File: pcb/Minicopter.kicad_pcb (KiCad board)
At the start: 2 copper layers, 57 parts, among them J1 USB_C_Receptacle_USB2.0_16P, J2 Conn_01x02, J3 Conn_01x02_Socket, J4 Conn_01x02_Socket, J5 Conn_01x02_Socket, J6 Conn_01x02_Socket, Q1 AO3401A, SW1 SS-12D00, T1 IRLML6344TRPBF, T2 IRLML6344TRPBF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

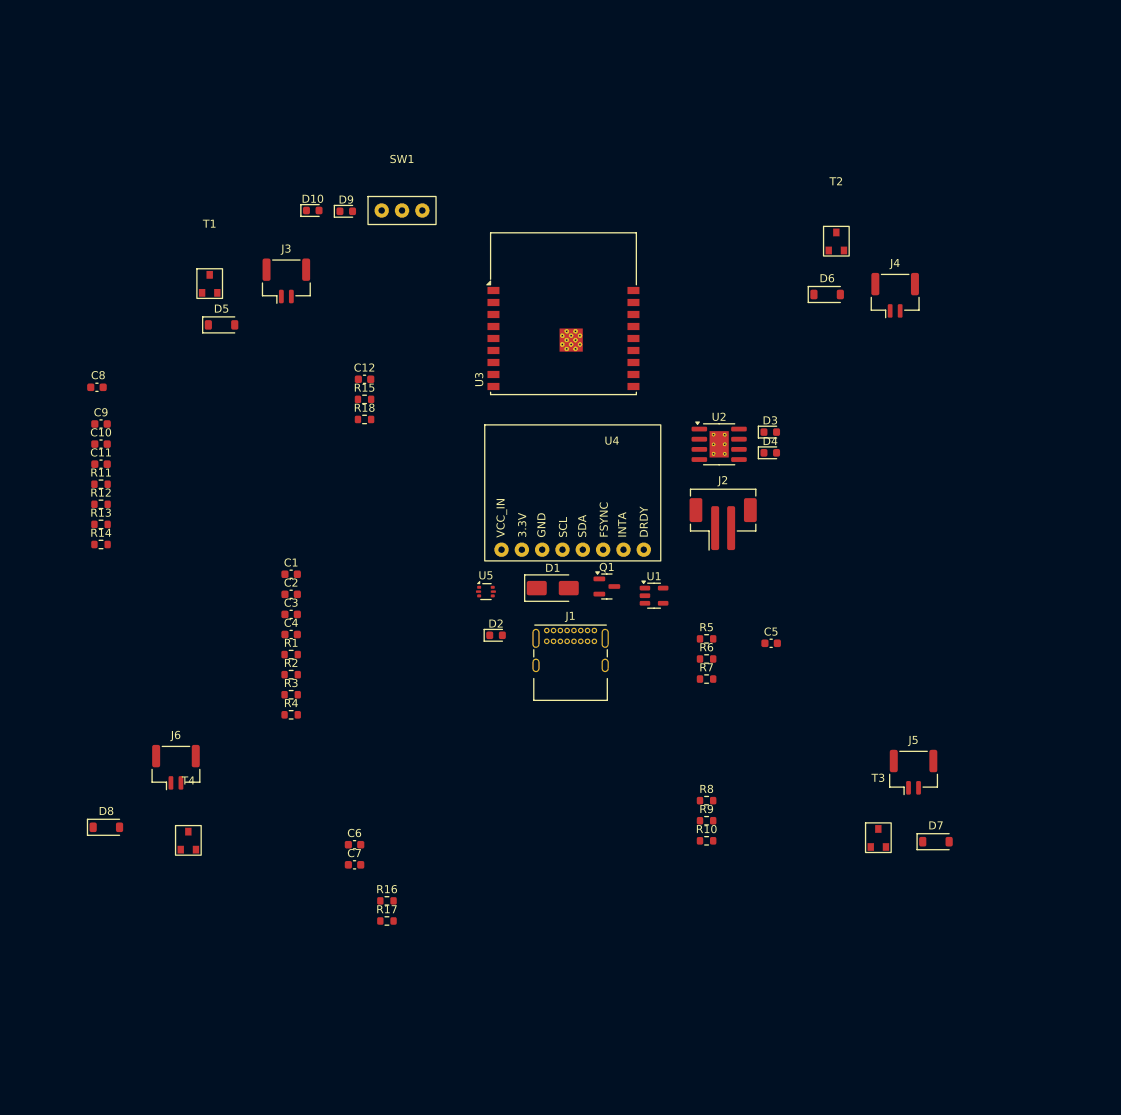
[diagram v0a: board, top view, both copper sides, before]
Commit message: without gnd
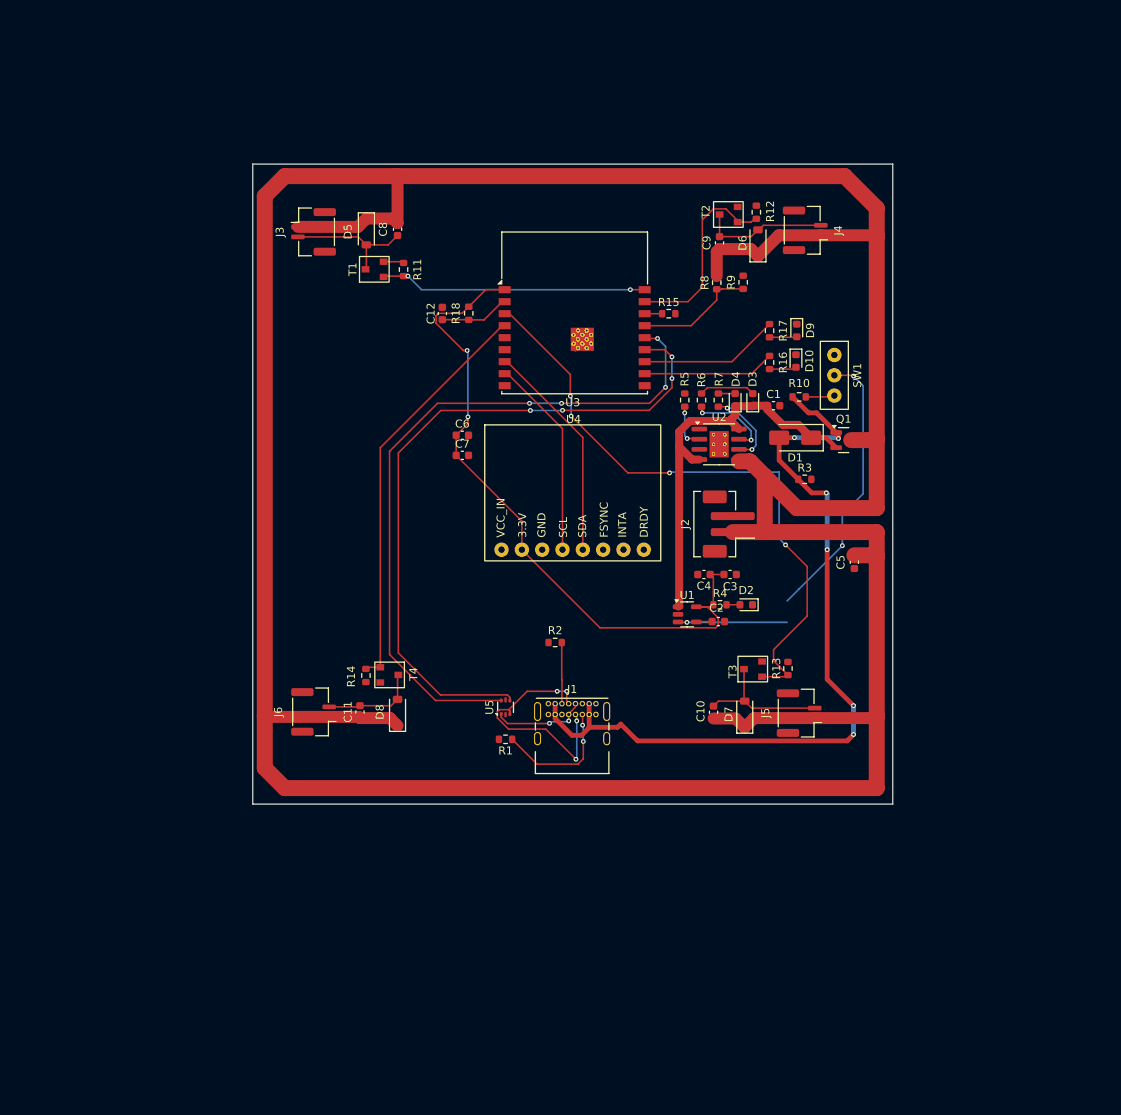
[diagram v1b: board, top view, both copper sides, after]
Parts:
- moved R12 89.7 mm to (173.9, 52.0), turned to 90 degrees
- moved R17 87.9 mm to (175.6, 66.8), turned to -90 degrees
- moved R13 87.7 mm to (177.9, 109.0), turned to 90 degrees
- moved C10 83.6 mm to (168.6, 114.5), turned to 90 degrees
- moved R16 82.6 mm to (175.6, 70.8), turned to -90 degrees
- moved C9 80.6 mm to (169.3, 55.8), turned to 90 degrees
- moved R3 69.6 mm to (180.0, 85.4)
- moved R9 67.5 mm to (172.3, 60.8), turned to -90 degrees
- moved R8 64.8 mm to (169.0, 60.8), turned to -90 degrees
- moved C1 63.9 mm to (176.1, 76.2)
- moved D10 63.3 mm to (178.9, 70.6), turned to -90 degrees
- moved D9 58.2 mm to (179.0, 66.8), turned to -90 degrees
- moved SW1 57.8 mm to (183.7, 72.4), turned to -90 degrees
- moved R10 56.7 mm to (179.3, 75.1)
- moved R4 55.3 mm to (169.4, 101.1)
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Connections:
- C1 pad 1: VBUS -> +5V
- D1 pad 1: VBUS -> +5V
- D1 pad 2: +5V -> VBUS
- J1 pad A4: +5V -> VBUS
- J1 pad A9: +5V -> VBUS
- J1 pad B4: +5V -> VBUS
- J1 pad B9: +5V -> VBUS
- Q1 pad 1: +5V -> VBUS
- Q1 pad 2: VBUS -> +5V
- R3 pad 1: +5V -> VBUS
- U1 pad 1: VBUS -> +5V
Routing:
- net +BATT: track 0.00 -> 430.9 mm
- net VBUS: track 0.00 -> 102.4 mm, vias 0 -> 6
- net /microcontroller/USBD+: track 0.00 -> 88.0 mm, vias 0 -> 4
- net /microcontroller/USBD-: track 0.00 -> 87.2 mm, vias 0 -> 4
- net +3V3: track 0.00 -> 86.0 mm, vias 0 -> 2
- net /microcontroller/MTR3: track 0.00 -> 78.2 mm, vias 0 -> 4
- net /microcontroller/MTR4: track 0.00 -> 51.2 mm
- net +5V: track 0.00 -> 50.7 mm
- net /battery control/LDO_EN: track 0.00 -> 48.6 mm, vias 0 -> 3
- net /microcontroller/MTR1: track 0.00 -> 33.4 mm, vias 0 -> 2
- net Net-(J1-D+-PadA6): track 0.00 -> 30.5 mm, vias 0 -> 4
- net /microcontroller/SDA: track 0.00 -> 27.7 mm
- net /microcontroller/SCL: track 0.00 -> 25.2 mm
- net /microcontroller/MTR2: track 0.00 -> 24.4 mm
- net /microcontroller/LED_BLUE: track 0.00 -> 17.6 mm
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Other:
- board outline added: 80 x 80 mm

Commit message: donedone
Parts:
- moved R2 4.60 mm to (148.7, 110.4)
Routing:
- net GND: track 3.82 -> 408.5 mm, vias 0 -> 16
- net Net-(J1-CC1): track 7.66 -> 2.92 mm
- net Net-(J1-D+-PadA6): track 30.5 -> 34.2 mm, vias 4 -> 2
- net /battery control/LDO_EN: track 48.6 -> 51.3 mm, vias 3 -> 4
- added copper zone on B.Cu, net GND

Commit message: oops now done hopefully
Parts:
- moved C11 9.39 mm to (123.1, 123.8)
- moved C3 9.39 mm to (169.4, 106.6)
- moved C4 9.39 mm to (166.1, 106.6)
- moved D10 9.39 mm to (177.6, 79.9)
- moved D3 9.39 mm to (172.2, 84.8)
- moved D4 9.39 mm to (170.0, 84.8)
- moved R10 9.39 mm to (178.0, 84.4)
- moved R13 9.39 mm to (176.6, 118.4)
- moved R14 9.39 mm to (123.8, 119.2)
- moved D8 9.39 mm to (127.8, 123.9)
- moved J6 9.39 mm to (117.3, 123.8)
- moved T4 9.39 mm to (125.1, 119.2)
- moved C12 9.39 mm to (133.4, 74.0)
- moved C2 9.39 mm to (167.9, 112.5)
- moved C7 9.39 mm to (135.9, 91.7)
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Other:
- board size 80 x 80 mm -> 136.1 x 135.4 mm
